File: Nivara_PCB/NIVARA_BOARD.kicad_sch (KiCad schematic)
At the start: 3 parts, among them U1 ESP32-S3-WROOM-1

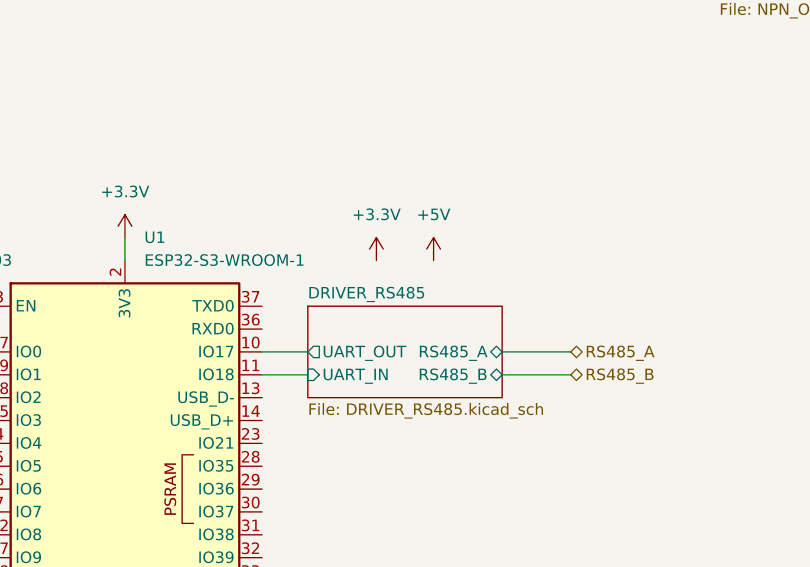
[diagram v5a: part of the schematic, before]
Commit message: Ajuste de RS-485 y protección de alimentación contra cortocircuito y sobre voltaje.
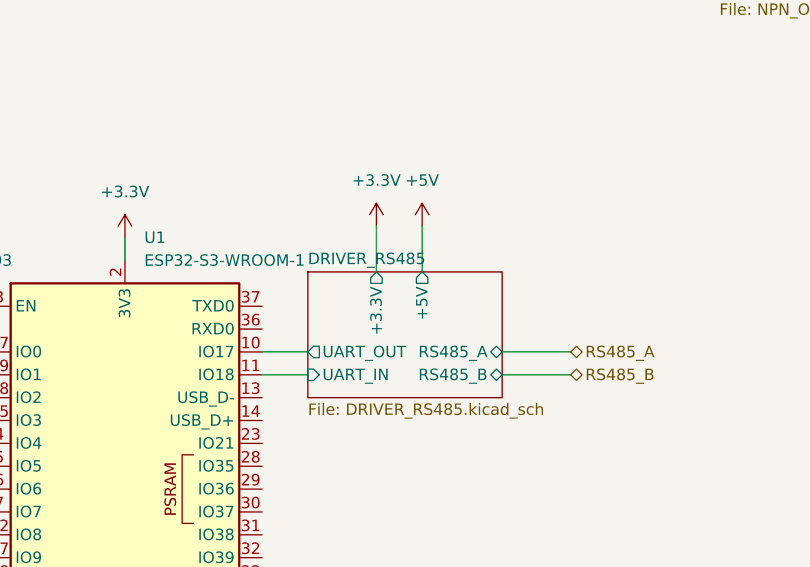
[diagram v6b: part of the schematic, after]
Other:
- sheet DRIVER_RS485 ports: added +3.3V, +5V; removed none
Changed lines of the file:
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@@
+	(wire
+		(pts
+			(xy 180.34 67.31) (xy 180.34 72.39)
+		)
+		(stroke
+			(width 0)
+			(type default)
+		)
+	)
 	(wire
 		(pts
@@
 		(pts
 			(xy 39.37 91.44) (xy 39.37 95.25)
+		)
+		(stroke
+			(width 0)
+			(type default)
+		)
+	)
+	(wire
+		(pts
+			(xy 175.26 67.31) (xy 175.26 72.39)
 		)
 		(stroke
@@
 	(symbol
 		(lib_id "power:+3.3V")
-		(at 175.26 71.12 0)
+		(at 175.26 67.31 0)
 		(unit 1)
 		(exclude_from_sim no)
@@
 		(fields_autoplaced yes)
 		(property "Reference" "#PWR030"
-			(at 175.26 74.93 0)
+			(at 175.26 71.12 0)
 			(effects
 				(font
@@
 		)
 		(property "Value" "+3.3V"
-			(at 175.26 66.04 0)
+			(at 175.26 62.23 0)
 			(effects
 				(font
@@
 		)
 		(property "Footprint" ""
-			(at 175.26 71.12 0)
+			(at 175.26 67.31 0)
 			(effects
 				(font
@@
 		)
 		(property "Datasheet" ""
-			(at 175.26 71.12 0)
+			(at 175.26 67.31 0)
 			(effects
 				(font
@@
 		)
 		(property "Description" "Power symbol creates a global label with name \"+3.3V\""
-			(at 175.26 71.12 0)
+			(at 175.26 67.31 0)
 			(effects
 				(font
@@
 	(symbol
 		(lib_id "power:+12V")
-		(at 181.61 71.12 0)
+		(at 180.34 67.31 0)
 		(unit 1)
 		(exclude_from_sim no)
@@
 		(fields_autoplaced yes)
 		(property "Reference" "#PWR031"
-			(at 181.61 74.93 0)
+			(at 180.34 71.12 0)
 			(effects
 				(font
@@
 		)
 		(property "Value" "+5V"
-			(at 181.61 66.04 0)
+			(at 180.34 62.23 0)
 			(effects
 				(font
@@
 		)
 		(property "Footprint" ""
-			(at 181.61 71.12 0)
+			(at 180.34 67.31 0)
 			(effects
 				(font
@@
 		)
 		(property "Datasheet" ""
-			(at 181.61 71.12 0)
+			(at 180.34 67.31 0)
 			(effects
 				(font
@@
 		)
 		(property "Description" "Power symbol creates a global label with name \"+12V\""
-			(at 181.61 71.12 0)
+			(at 180.34 67.31 0)
 			(effects
 				(font
@@
 	)
 	(sheet
-		(at 167.64 76.2)
-		(size 21.59 10.16)
+		(at 167.64 72.39)
+		(size 21.59 13.97)
 		(exclude_from_sim no)
 		(in_bom yes)
@@
 		)
 		(property "Sheetname" "DRIVER_RS485"
-			(at 167.64 75.4884 0)
+			(at 167.64 71.6784 0)
 			(effects
 				(font
@@
 			)
 		)
+		(pin "+3.3V" output
+			(at 175.26 72.39 90)
+			(effects
+				(font
+					(size 1.27 1.27)
+				)
+				(justify right)
+			)
+		)
+		(pin "+5V" output
+			(at 180.34 72.39 90)
+			(effects
+				(font
+					(size 1.27 1.27)
+				)
+				(justify right)
+			)
+		)
